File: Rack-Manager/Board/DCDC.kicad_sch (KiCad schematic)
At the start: 11 parts, among them U4 TLVM23625, U5 INA220

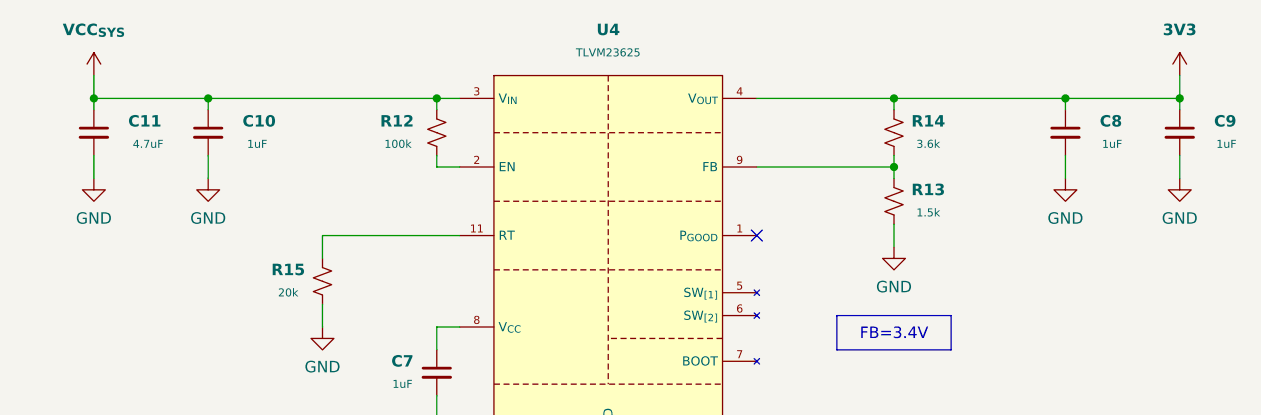
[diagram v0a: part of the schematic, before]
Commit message: Updated Texas Instruments and WIZnet KiCAD libraries. Continued with the schematics design.
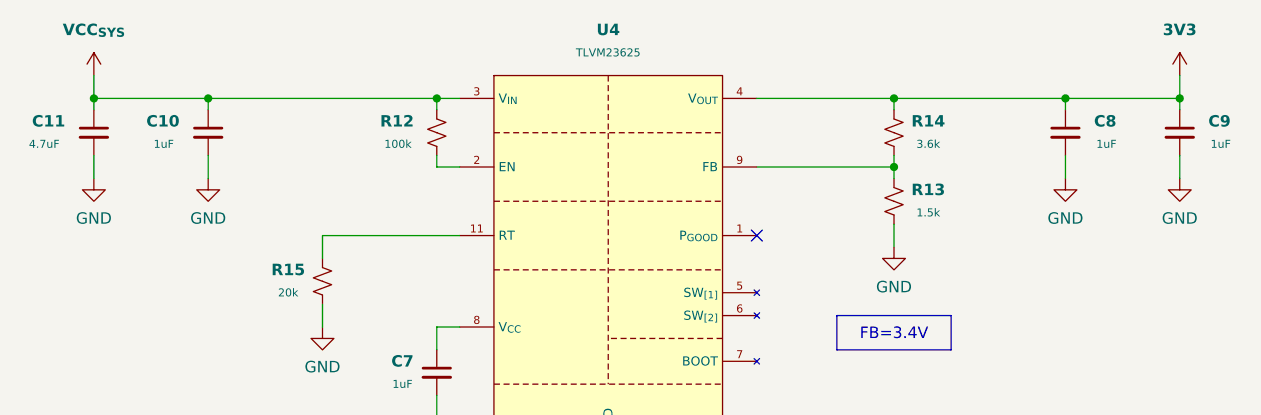
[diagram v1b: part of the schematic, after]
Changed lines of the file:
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@@
 		(dnp no)
 		(property "Reference" "C11"
-			(at 86.36 43.18 0)
+			(at 79.375 43.18 0)
 			(effects
 				(font
@@
 					(bold yes)
 				)
-				(justify left)
+				(justify right)
 			)
 		)
 		(property "Value" "4.7uF"
-			(at 86.868 45.72 0)
+			(at 78.74 45.72 0)
 			(effects
 				(font
 					(size 0.889 0.889)
 				)
-				(justify left)
+				(justify right)
 			)
 		)
@@
 		(dnp no)
 		(property "Reference" "C9"
-			(at 207.01 43.18 0)
+			(at 206.375 43.18 0)
 			(effects
 				(font
@@
 		)
 		(property "Value" "1uF"
-			(at 207.264 45.72 0)
+			(at 206.629 45.72 0)
 			(effects
 				(font
@@
 		(dnp no)
 		(property "Reference" "C10"
-			(at 99.06 43.18 0)
+			(at 92.075 43.18 0)
 			(effects
 				(font
@@
 					(bold yes)
 				)
-				(justify left)
+				(justify right)
 			)
 		)
 		(property "Value" "1uF"
-			(at 99.568 45.72 0)
+			(at 91.44 45.72 0)
 			(effects
 				(font
 					(size 0.889 0.889)
 				)
-				(justify left)
+				(justify right)
 			)
 		)
@@
 		(dnp no)
 		(property "Reference" "C8"
-			(at 194.31 43.18 0)
+			(at 193.675 43.18 0)
 			(effects
 				(font
@@
 		)
 		(property "Value" "1uF"
-			(at 194.564 45.72 0)
-			(effects
-				(font
+			(at 193.929 45.72 0)
+			(effects
+				(font

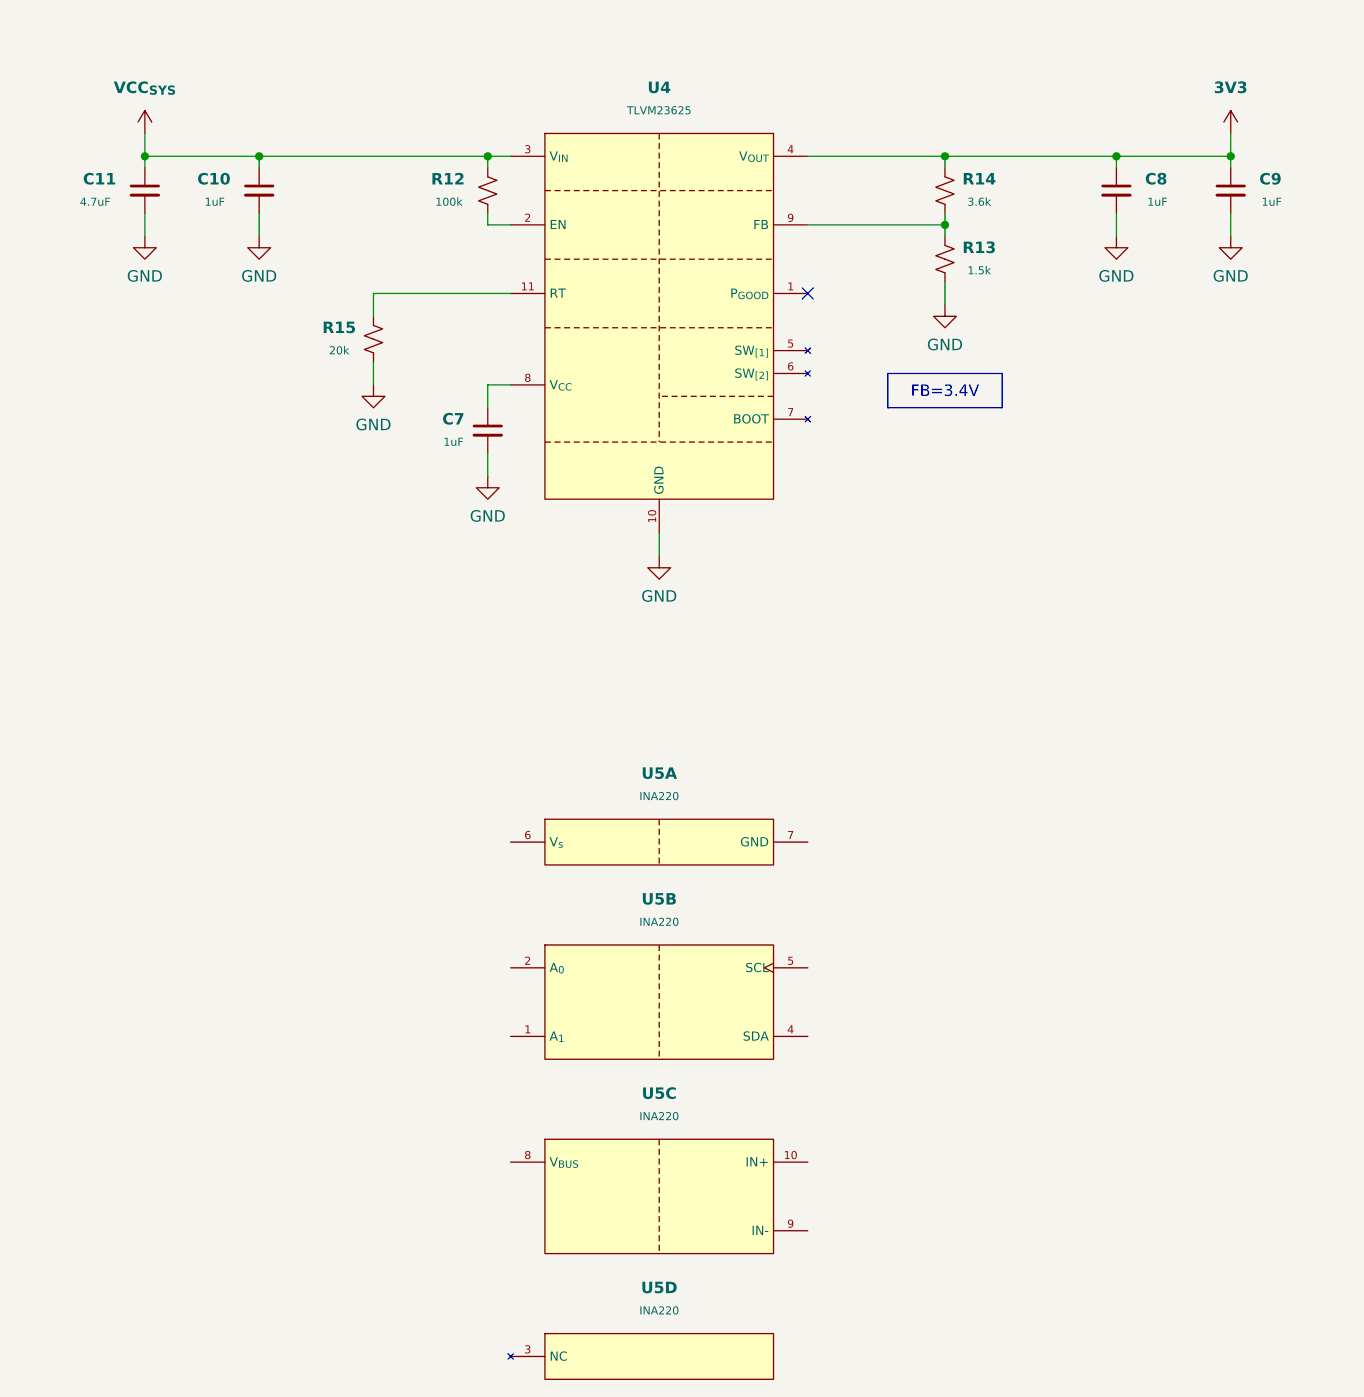
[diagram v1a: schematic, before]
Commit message: Updated Texas Instruments KiCAD library. Continued with the schematics design.
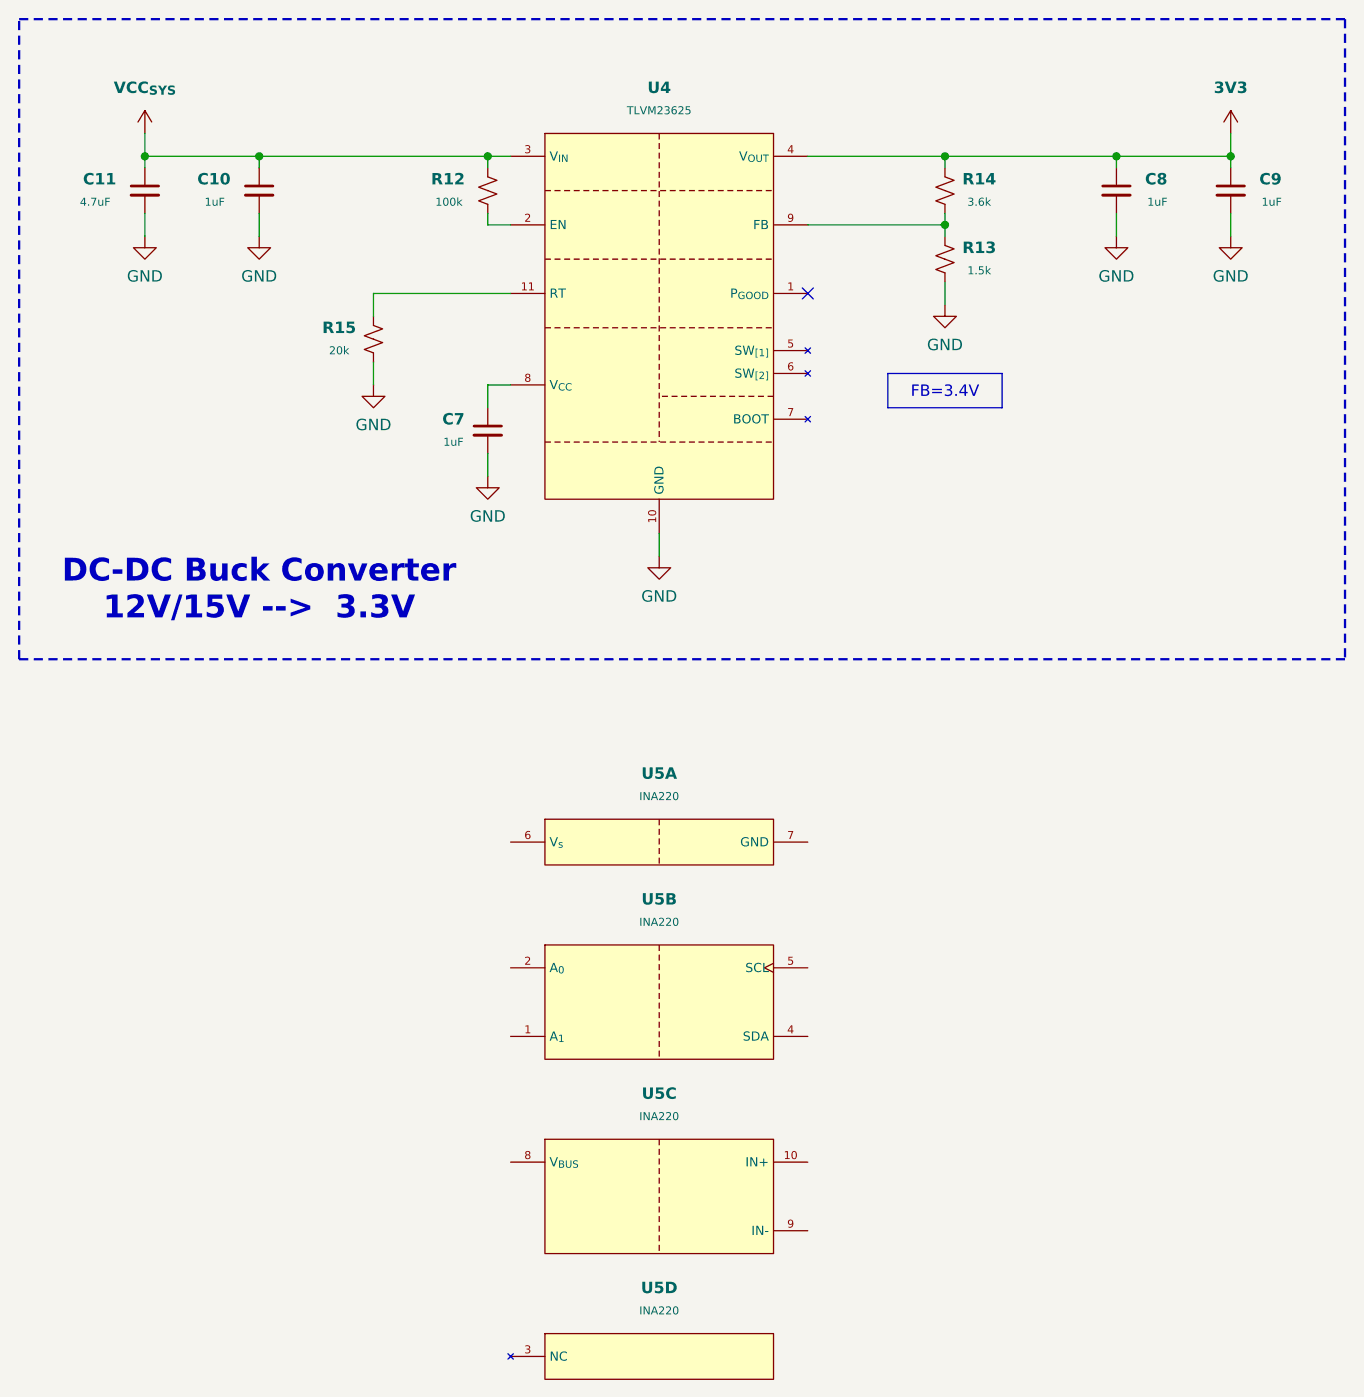
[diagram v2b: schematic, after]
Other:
- note added: "DC-DC Buck Converter 12V/15V --> 3.3V"
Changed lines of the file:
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@@
 		(comment 1 "Rack-Manager")
+	)
+	(rectangle
+		(start 68.58 25.4)
+		(end 215.9 96.52)
+		(stroke
+			(width 0.254)
+			(type dash)
+		)
+		(fill
+			(type none)
+		)
+	)
+	(text "DC-DC Buck Converter\n12V/15V -->  3.3V"
+		(exclude_from_sim no)
+		(at 95.25 88.9 0)
+		(effects
+			(font
+				(size 2.54 2.54)
+				(thickness 0.508)
+				(bold yes)
+			)
+		)
 	)
 	(text_box "FB=3.4V"

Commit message: Continued with the schematic drawing.
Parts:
- renumbered C7 to C11, C8 to C12, C9 to C13, C11 to C9
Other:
- note added: "DC-DC Buck Converter 12V/15V 3.3V"
- note added: "→"
- note removed: "DC-DC Buck Converter 12V/15V --> 3.3V"
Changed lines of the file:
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@@
 		)
 	)
-	(text "DC-DC Buck Converter\n12V/15V -->  3.3V"
+	(text "→"
+		(exclude_from_sim no)
+		(at 99.568 90.678 0)
+		(effects
+			(font
+				(size 5.08 5.08)
+				(thickness 0.635)
+			)
+		)
+	)
+	(text "DC-DC Buck Converter\n12V/15V      3.3V"
 		(exclude_from_sim no)
 		(at 95.25 88.9 0)
@@
 		(on_board yes)
 		(dnp no)
-		(property "Reference" "C11"
+		(property "Reference" "C9"
 			(at 79.375 43.18 0)
 			(effects
@@
 			(project "Rack-Manager"
 				(path "/5d42174d-da49-4bca-870b-353868af7168/04b4a11e-cbcf-414e-a904-9ef8b3f12c1f"
-					(reference "C11")
+					(reference "C9")
 					(unit 1)
 				)
@@
 		(on_board yes)
 		(dnp no)
-		(property "Reference" "C9"
+		(property "Reference" "C13"
 			(at 206.375 43.18 0)
 			(effects
@@
 			(project "Rack-Manager"
 				(path "/5d42174d-da49-4bca-870b-353868af7168/04b4a11e-cbcf-414e-a904-9ef8b3f12c1f"
-					(reference "C9")
+					(reference "C13")
 					(unit 1)
 				)
@@
 		(on_board yes)
 		(dnp no)
-		(property "Reference" "C7"
+		(property "Reference" "C11"
 			(at 116.84 69.85 0)
 			(effects
@@
 			(project "Rack-Manager"
 				(path "/5d42174d-da49-4bca-870b-353868af7168/04b4a11e-cbcf-414e-a904-9ef8b3f12c1f"
-					(reference "C7")
+					(reference "C11")
 					(unit 1)
 				)
@@
 		(on_board yes)
 		(dnp no)
-		(property "Reference" "C8"
+		(property "Reference" "C12"
 			(at 193.675 43.18 0)
 			(effects
@@
 			(project "Rack-Manager"
 				(path "/5d42174d-da49-4bca-870b-353868af7168/04b4a11e-cbcf-414e-a904-9ef8b3f12c1f"
-					(reference "C8")
+					(reference "C12")
 					(unit 1)
 				)

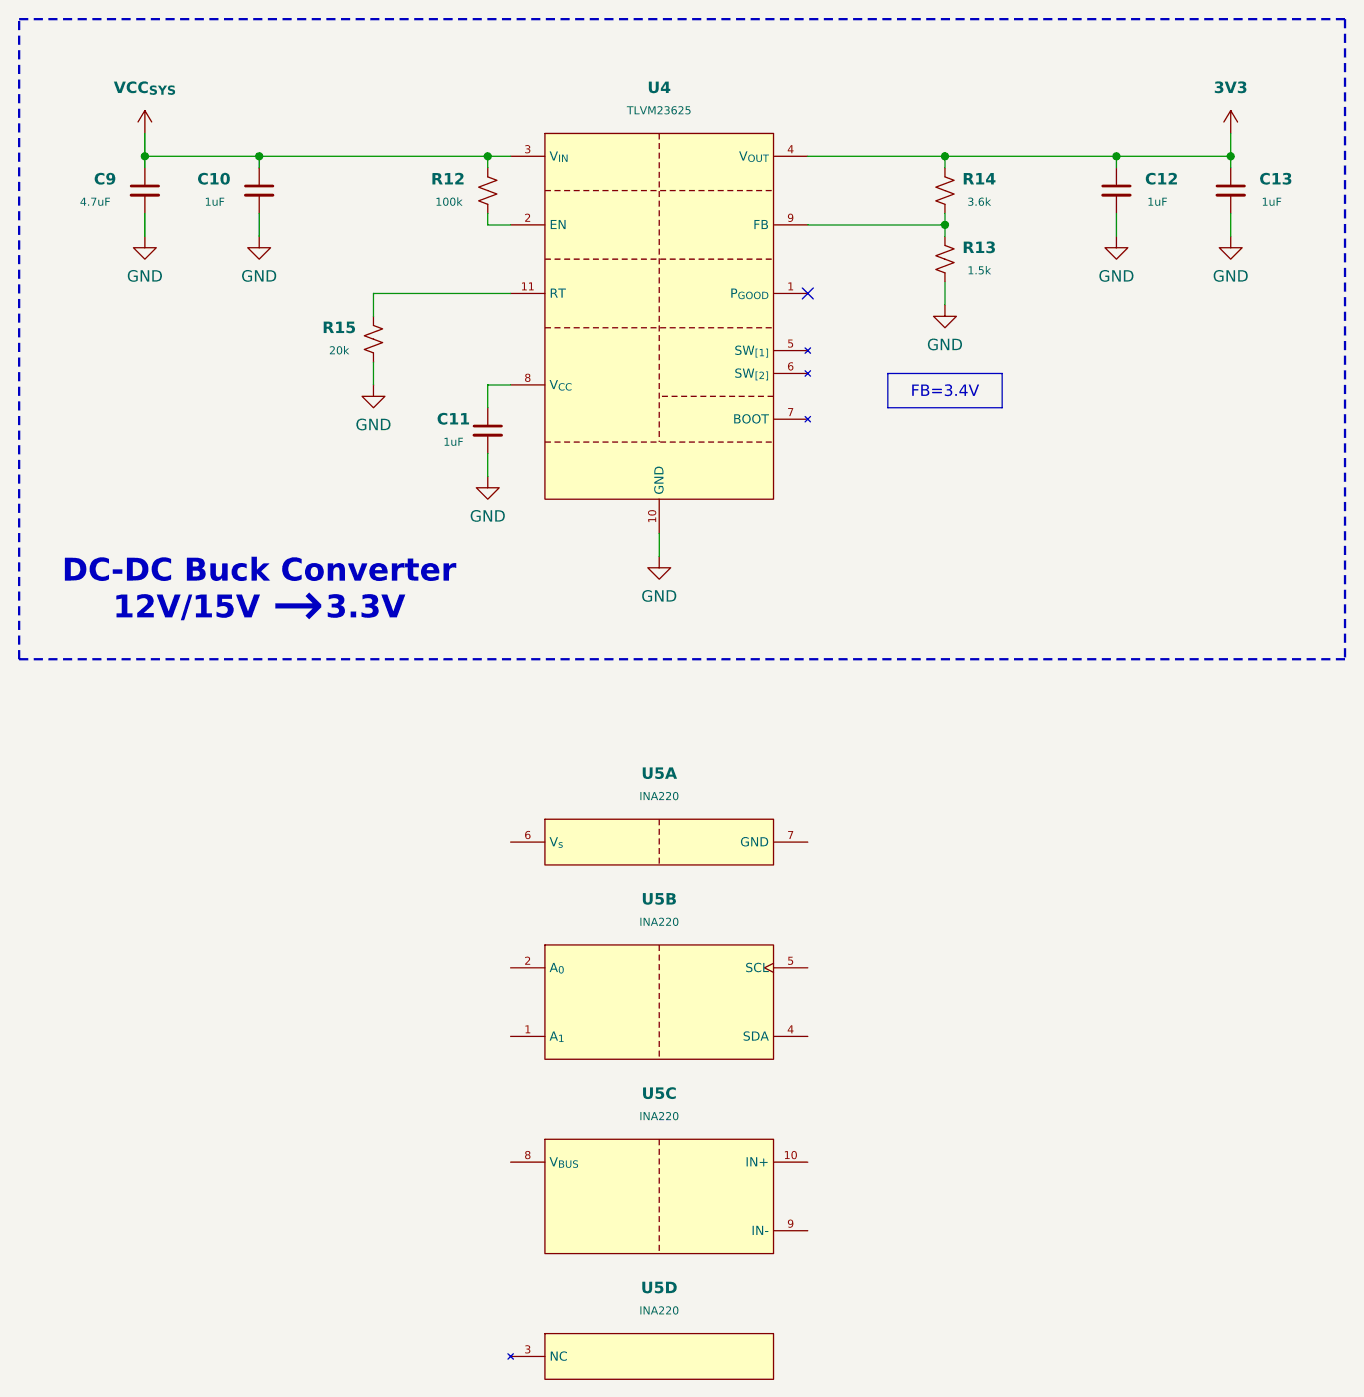
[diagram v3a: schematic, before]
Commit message: Added Bourns library, updated Texas Instruments library, continued with schematic drawing.
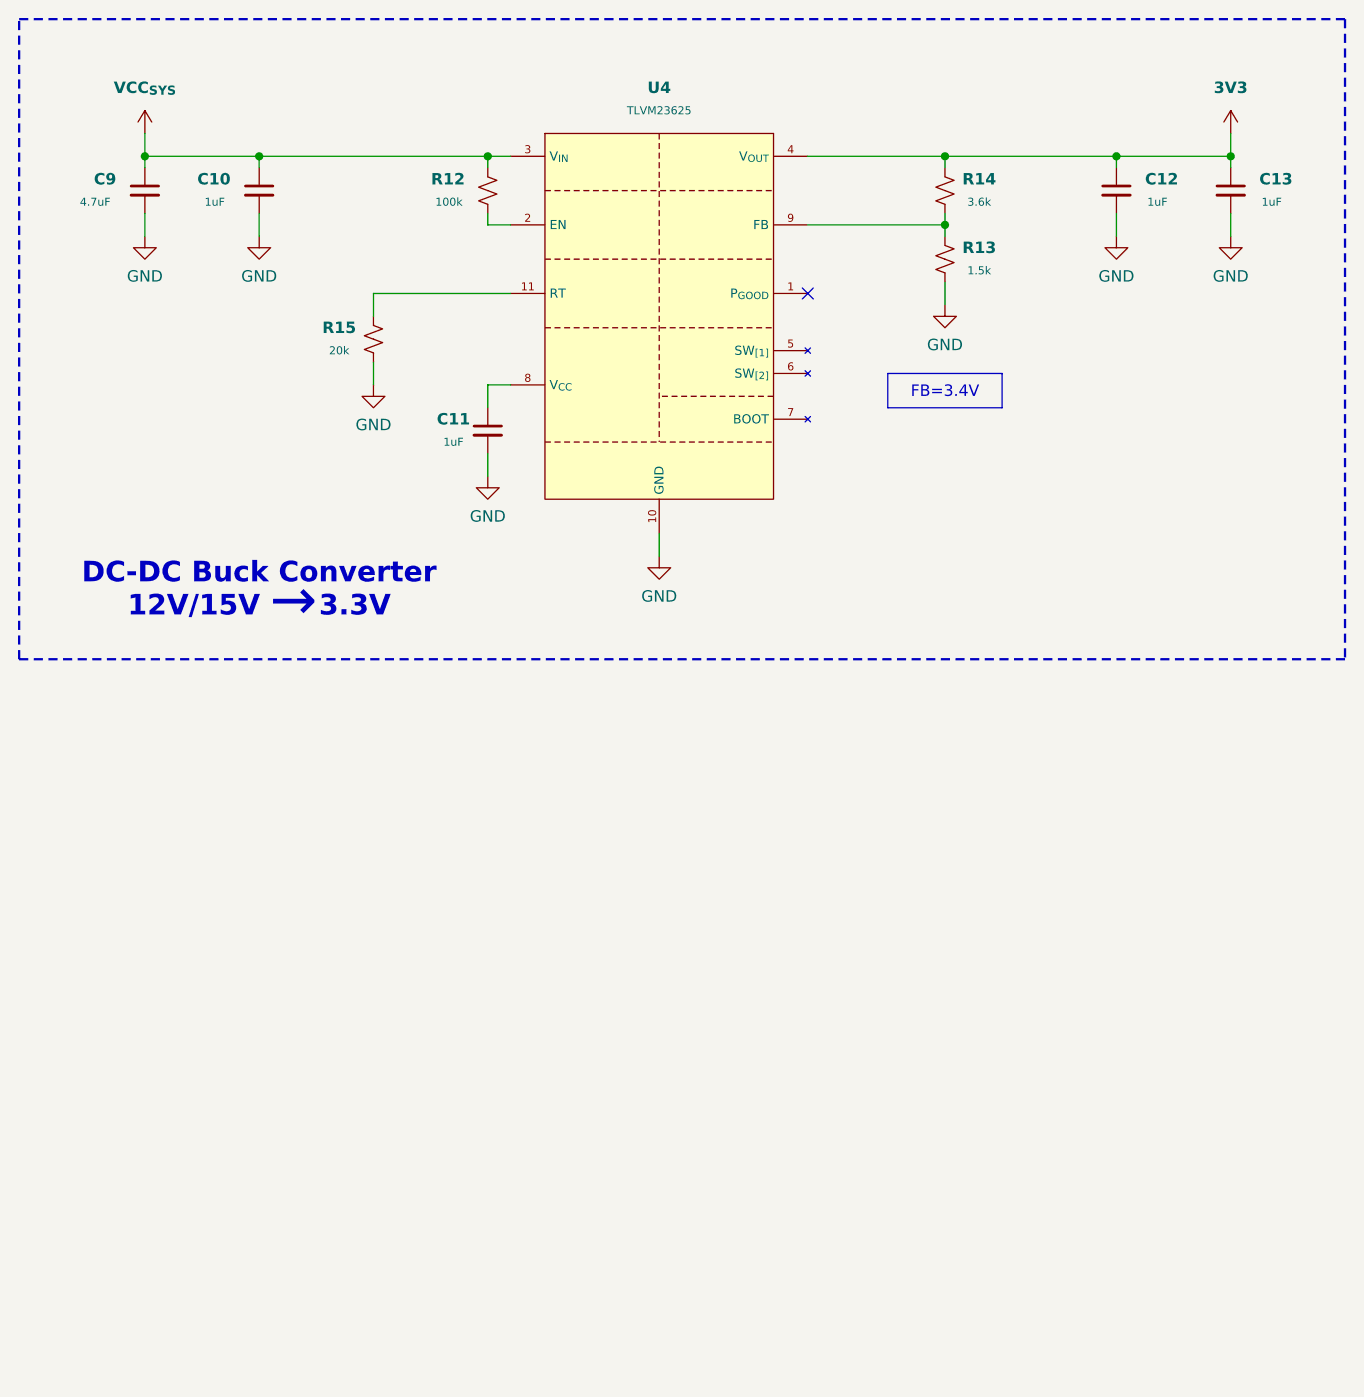
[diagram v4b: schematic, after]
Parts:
- removed U5: INA220, Texas Instruments:DGS0010A, symbol Texas Instruments:INA220
